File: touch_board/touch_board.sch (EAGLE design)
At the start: 43 parts, among them IC1 PIC18F47K42-I_PT, IC2 MAX203EEWP, K1 G6K-2P, X1 RS-232-1, X2 RS-232-2, X3 POWER, X4 GLORY, X5 Relay conn

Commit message: update
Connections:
- removed net N$59: C7.1, D2.A, R4.1
- new net N$62: C7.1, D2.A, R4.1, S3.1, S3.2, SV3.1
- net N$2: no longer S3.1, S3.2, SV3.1
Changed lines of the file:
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@@
 <wire x1="83.82" y1="-40.64" x2="83.82" y2="-43.18" width="0.1524" layer="91"/>
 <pinref part="SV2" gate="G$1" pin="4"/>
-<wire x1="83.82" y1="-20.32" x2="132.08" y2="-20.32" width="0.1524" layer="91"/>
+<wire x1="83.82" y1="-20.32" x2="137.16" y2="-20.32" width="0.1524" layer="91"/>
 <junction x="83.82" y="-20.32"/>
 <junction x="137.16" y="-20.32"/>
-<wire x1="132.08" y1="-20.32" x2="137.16" y2="-20.32" width="0.1524" layer="91"/>
-<wire x1="132.08" y1="-20.32" x2="132.08" y2="-30.48" width="0.1524" layer="91"/>
-<pinref part="SV3" gate="G$1" pin="1"/>
-<wire x1="132.08" y1="-30.48" x2="132.08" y2="-35.56" width="0.1524" layer="91"/>
-<wire x1="132.08" y1="-35.56" x2="137.16" y2="-35.56" width="0.1524" layer="91"/>
-<junction x="137.16" y="-35.56"/>
-<junction x="132.08" y="-20.32"/>
-<pinref part="S3" gate="G$1" pin="2"/>
-<pinref part="S3" gate="G$1" pin="1"/>
-<wire x1="165.1" y1="-55.88" x2="165.1" y2="-53.34" width="0.1524" layer="91"/>
-<wire x1="165.1" y1="-53.34" x2="165.1" y2="-50.8" width="0.1524" layer="91"/>
-<wire x1="165.1" y1="-50.8" x2="152.4" y2="-50.8" width="0.1524" layer="91"/>
-<wire x1="152.4" y1="-50.8" x2="152.4" y2="-30.48" width="0.1524" layer="91"/>
-<wire x1="152.4" y1="-30.48" x2="132.08" y2="-30.48" width="0.1524" layer="91"/>
-<junction x="132.08" y="-30.48"/>
-<junction x="165.1" y="-53.34"/>
-<junction x="165.1" y="-55.88"/>
 <pinref part="D2" gate="G$1" pin="C"/>
 <wire x1="71.12" y1="-20.32" x2="76.2" y2="-20.32" width="0.1524" layer="91"/>
@@
 </segment>
 </net>
-<net name="N$59" class="0">
-<segment>
+<net name="N$62" class="0">
+<segment>
+<pinref part="SV3" gate="G$1" pin="1"/>
+<junction x="137.16" y="-35.56"/>
+<wire x1="132.08" y1="-35.56" x2="137.16" y2="-35.56" width="0.1524" layer="91"/>
+<wire x1="132.08" y1="-35.56" x2="132.08" y2="-27.94" width="0.1524" layer="91"/>
+<wire x1="132.08" y1="-27.94" x2="152.4" y2="-27.94" width="0.1524" layer="91"/>
+<pinref part="S3" gate="G$1" pin="1"/>
+<pinref part="S3" gate="G$1" pin="2"/>
+<junction x="165.1" y="-55.88"/>
+<wire x1="165.1" y1="-55.88" x2="165.1" y2="-53.34" width="0.1524" layer="91"/>
+<junction x="165.1" y="-53.34"/>
+<wire x1="165.1" y1="-53.34" x2="165.1" y2="-50.8" width="0.1524" layer="91"/>
+<wire x1="165.1" y1="-50.8" x2="152.4" y2="-50.8" width="0.1524" layer="91"/>
+<wire x1="152.4" y1="-27.94" x2="152.4" y2="-50.8" width="0.1524" layer="91"/>
+<wire x1="152.4" y1="-50.8" x2="152.4" y2="-68.58" width="0.1524" layer="91"/>
+<wire x1="152.4" y1="-68.58" x2="53.34" y2="-68.58" width="0.1524" layer="91"/>
 <pinref part="C7" gate="G$1" pin="1"/>
 <pinref part="R4" gate="G$1" pin="1"/>
@@
 <pinref part="D2" gate="G$1" pin="A"/>
 <junction x="66.04" y="-20.32"/>
-</segment>
-</net>
+<wire x1="53.34" y1="-68.58" x2="53.34" y2="-20.32" width="0.1524" layer="91"/>
+<junction x="152.4" y="-50.8"/>
+</segment>
+</net>

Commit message: update
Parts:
- added C10: 0.1, rcl:C-USC0805
- added LED1: PWR ON, led:LEDCHIPLED_1206
- added PAD1: LCD9, wirepad:SMD2
- added PAD2: LCD10, wirepad:SMD2
- added R8: 220, rcl:R-US_R0805
- added SV8: LCD, con-lstb:MA10-1
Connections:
- new net N$63: IC1.RC4, SV5.5, SV8.1
- new net N$66: PAD1.P, SV8.9
- new net N$67: PAD2.P, SV8.10
- net N$33: now also SV8.6
- net N$34: now also SV8.4
- net N$35: now also SV8.5
- net N$36: now also SV8.3
- net N$37: now also LED1.A, R8.2; no longer IC1.RC4, SV5.5
- net N$38: now also SV8.2
- net VDD: now also C10.1, R8.1, SV8.7
- net VSS: now also C10.2, LED1.C, SV8.8

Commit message: update
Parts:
- added SV9: USBH, con-lstb:MA03-1
- added X6: MINI-USB-UX60A-MB-5ST, con-hirose:MINI-USB-UX60A-MB-5ST
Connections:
- new net N$59: SV9.3, X6.2
- new net N$61: SV9.2, X6.3
- new net N$64: SV9.1, X6.4
- net N$60: now also X6.1
- net VSS: now also X6.5
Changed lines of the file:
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@@
 <part name="LED1" library="led" library_urn="urn:adsk.eagle:library:259" deviceset="LED" device="CHIPLED_1206" package3d_urn="urn:adsk.eagle:package:15823/2" value="PWR ON"/>
 <part name="VSS26" library="supply1" library_urn="urn:adsk.eagle:library:371" deviceset="VSS" device=""/>
+<part name="VSS27" library="supply1" library_urn="urn:adsk.eagle:library:371" deviceset="VSS" device=""/>
+<part name="SV9" library="con-lstb" library_urn="urn:adsk.eagle:library:162" deviceset="MA03-1" device="" package3d_urn="urn:adsk.eagle:package:8339/1" value="USBH"/>
+<part name="X6" library="con-hirose" library_urn="urn:adsk.eagle:library:152" deviceset="MINI-USB-" device="UX60A-MB-5ST" package3d_urn="urn:adsk.eagle:package:7263/1"/>
 </parts>
 <sheets>
@@
 <instance part="VSS26" gate="G$1" x="104.14" y="-66.04" smashed="yes" rot="R90">
 <attribute name="VALUE" x="109.22" y="-68.58" size="1.778" layer="96" rot="R180"/>
+</instance>
+<instance part="VSS27" gate="G$1" x="182.88" y="-27.94" smashed="yes">
+<attribute name="VALUE" x="180.34" y="-33.02" size="1.778" layer="96" rot="R90"/>
+</instance>
+<instance part="SV9" gate="G$1" x="170.18" y="-20.32" smashed="yes">
+<attribute name="VALUE" x="168.91" y="-27.94" size="1.778" layer="96"/>
+<attribute name="NAME" x="168.91" y="-14.478" size="1.778" layer="95"/>
+</instance>
+<instance part="X6" gate="G$1" x="187.96" y="-20.32" smashed="yes">
+<attribute name="NAME" x="185.42" y="-8.89" size="1.778" layer="95"/>
+<attribute name="VALUE" x="198.12" y="-27.94" size="1.778" layer="96" rot="R90"/>
 </instance>
 </instances>
@@
 <pinref part="VSS26" gate="G$1" pin="VSS"/>
 <junction x="101.6" y="-66.04"/>
+</segment>
+<segment>
+<pinref part="VSS27" gate="G$1" pin="VSS"/>
+<pinref part="X6" gate="G$1" pin="5"/>
+<junction x="182.88" y="-25.4"/>
 </segment>
 </net>
@@
 <pinref part="D1" gate="G$1" pin="C"/>
 <junction x="127" y="-55.88"/>
+<wire x1="182.88" y1="-15.24" x2="160.02" y2="-7.62" width="0.1524" layer="91"/>
+<wire x1="160.02" y1="-7.62" x2="160.02" y2="-45.72" width="0.1524" layer="91"/>
+<wire x1="160.02" y1="-45.72" x2="127" y2="-45.72" width="0.1524" layer="91"/>
+<wire x1="127" y1="-45.72" x2="127" y2="-35.56" width="0.1524" layer="91"/>
+<wire x1="127" y1="-35.56" x2="109.22" y2="-35.56" width="0.1524" layer="91"/>
+<wire x1="109.22" y1="-35.56" x2="109.22" y2="-43.18" width="0.1524" layer="91"/>
+<pinref part="X6" gate="G$1" pin="1"/>
+<junction x="182.88" y="-15.24"/>
 </segment>
 </net>
@@
 </segment>
 </net>
+<net name="N$59" class="0">
+<segment>
+<pinref part="SV9" gate="G$1" pin="3"/>
+<wire x1="182.88" y1="-17.78" x2="177.8" y2="-17.78" width="0.1524" layer="91"/>
+<junction x="177.8" y="-17.78"/>
+<pinref part="X6" gate="G$1" pin="2"/>
+<junction x="182.88" y="-17.78"/>
+</segment>
+</net>
+<net name="N$61" class="0">
+<segment>
+<pinref part="SV9" gate="G$1" pin="2"/>
+<wire x1="182.88" y1="-20.32" x2="177.8" y2="-20.32" width="0.1524" layer="91"/>
+<junction x="177.8" y="-20.32"/>
+<pinref part="X6" gate="G$1" pin="3"/>
+<junction x="182.88" y="-20.32"/>
+</segment>
+</net>
+<net name="N$64" class="0">
+<segment>
+<pinref part="SV9" gate="G$1" pin="1"/>
+<wire x1="182.88" y1="-22.86" x2="177.8" y2="-22.86" width="0.1524" layer="91"/>
+<junction x="177.8" y="-22.86"/>
+<pinref part="X6" gate="G$1" pin="4"/>
+<junction x="182.88" y="-22.86"/>
+</segment>
+</net>

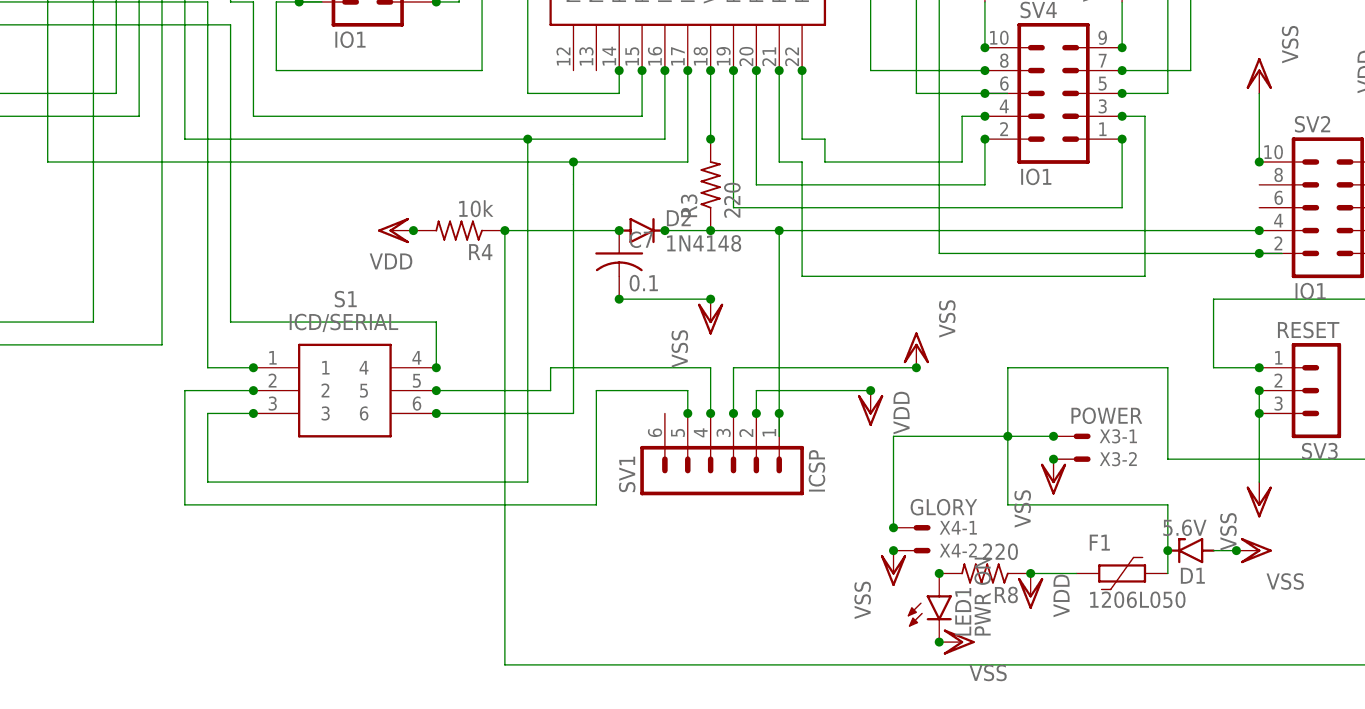
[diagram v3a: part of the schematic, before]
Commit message: update and fix switch pins on pcb
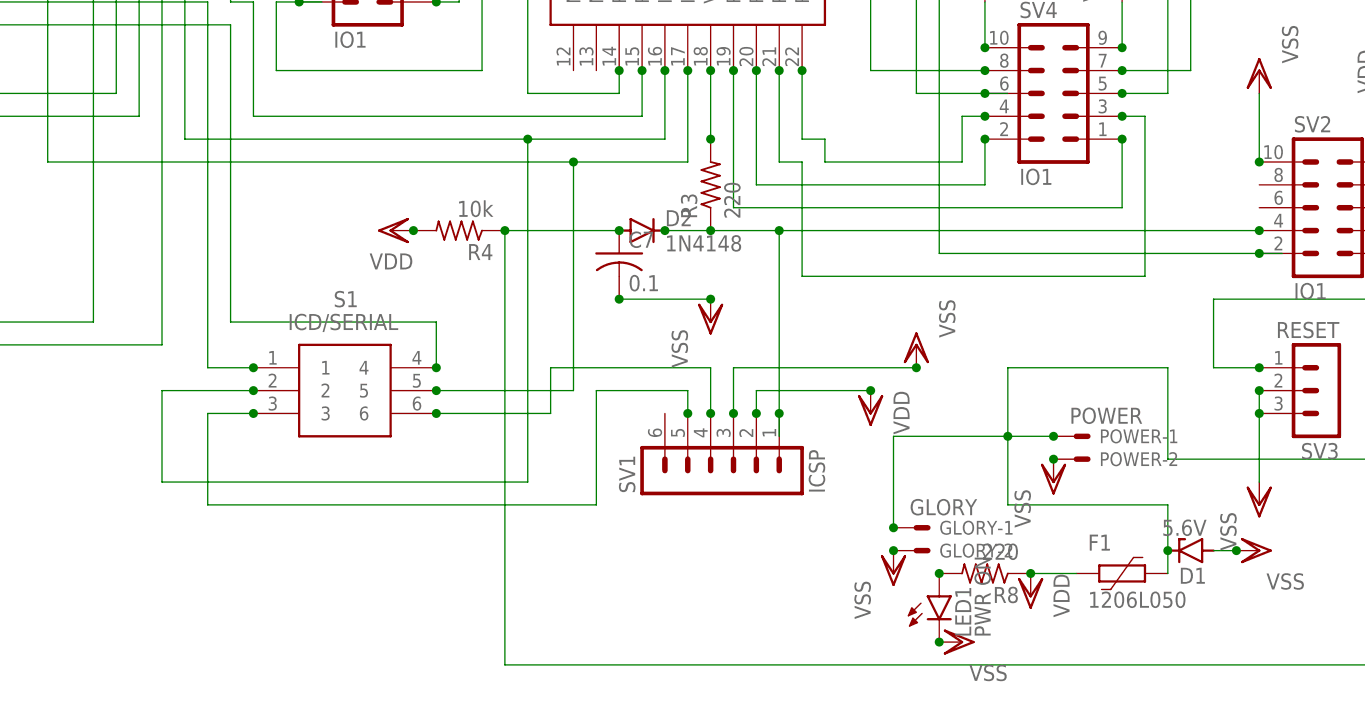
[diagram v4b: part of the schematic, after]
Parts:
- renumbered X3 to POWER, X4 to GLORY
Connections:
- removed net N$24: S1.2, SV1.5
- new net N$65: S1.3, SV1.5
- net N$23: now also S1.6; no longer S1.5
- net N$6: now also S1.5; no longer S1.6
- net N$7: now also S1.2; no longer S1.3
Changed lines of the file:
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@@
 <part name="P+2" library="supply1" library_urn="urn:adsk.eagle:library:371" deviceset="VCC" device=""/>
 <part name="P+3" library="supply1" library_urn="urn:adsk.eagle:library:371" deviceset="VCC" device=""/>
-<part name="X3" library="con-molex" library_urn="urn:adsk.eagle:library:165" deviceset="22-23-2021" device="" package3d_urn="urn:adsk.eagle:package:8078633/1" value="POWER"/>
+<part name="POWER" library="con-molex" library_urn="urn:adsk.eagle:library:165" deviceset="22-23-2021" device="" package3d_urn="urn:adsk.eagle:package:8078633/1" value="POWER"/>
 <part name="VSS13" library="supply1" library_urn="urn:adsk.eagle:library:371" deviceset="VSS" device=""/>
 <part name="C8" library="rcl" library_urn="urn:adsk.eagle:library:334" deviceset="C-US" device="C0805" package3d_urn="urn:adsk.eagle:package:23617/2" value="0.1"/>
@@
 <part name="VSS19" library="supply1" library_urn="urn:adsk.eagle:library:371" deviceset="VSS" device=""/>
 <part name="VDD12" library="supply1" library_urn="urn:adsk.eagle:library:371" deviceset="VDD" device=""/>
-<part name="X4" library="con-molex" library_urn="urn:adsk.eagle:library:165" deviceset="22-23-2021" device="" package3d_urn="urn:adsk.eagle:package:8078633/1" value="GLORY"/>
+<part name="GLORY" library="con-molex" library_urn="urn:adsk.eagle:library:165" deviceset="22-23-2021" device="" package3d_urn="urn:adsk.eagle:package:8078633/1" value="GLORY"/>
 <part name="VSS20" library="supply1" library_urn="urn:adsk.eagle:library:371" deviceset="VSS" device=""/>
 <part name="K1" library="relay" library_urn="urn:adsk.eagle:library:339" deviceset="G6K" device="-2P" package3d_urn="urn:adsk.eagle:package:24346/1"/>
@@
 <attribute name="VALUE" x="-10.16" y="-27.94" size="1.778" layer="96" rot="R90"/>
 </instance>
-<instance part="X3" gate="-1" x="116.84" y="-43.18" smashed="yes">
+<instance part="POWER" gate="-1" x="116.84" y="-43.18" smashed="yes">
 <attribute name="NAME" x="119.38" y="-43.942" size="1.524" layer="95"/>
 <attribute name="VALUE" x="116.078" y="-41.783" size="1.778" layer="96"/>
 </instance>
-<instance part="X3" gate="-2" x="116.84" y="-45.72" smashed="yes">
+<instance part="POWER" gate="-2" x="116.84" y="-45.72" smashed="yes">
 <attribute name="NAME" x="119.38" y="-46.482" size="1.524" layer="95"/>
 </instance>
@@
 <attribute name="VALUE" x="43.18" y="15.24" size="1.778" layer="96" rot="R90"/>
 </instance>
-<instance part="X4" gate="-1" x="99.06" y="-53.34" smashed="yes">
+<instance part="GLORY" gate="-1" x="99.06" y="-53.34" smashed="yes">
 <attribute name="NAME" x="101.6" y="-54.102" size="1.524" layer="95"/>
 <attribute name="VALUE" x="98.298" y="-51.943" size="1.778" layer="96"/>
 </instance>
-<instance part="X4" gate="-2" x="99.06" y="-55.88" smashed="yes">
+<instance part="GLORY" gate="-2" x="99.06" y="-55.88" smashed="yes">
 <attribute name="NAME" x="101.6" y="-56.642" size="1.524" layer="95"/>
 </instance>
@@
 </segment>
 <segment>
-<pinref part="X3" gate="-2" pin="S"/>
+<pinref part="POWER" gate="-2" pin="S"/>
 <pinref part="VSS13" gate="G$1" pin="VSS"/>
 <junction x="114.3" y="-45.72"/>
@@
 </segment>
 <segment>
-<pinref part="X4" gate="-2" pin="S"/>
+<pinref part="GLORY" gate="-2" pin="S"/>
 <pinref part="VSS20" gate="G$1" pin="VSS"/>
 <junction x="96.52" y="-55.88"/>
@@
 <wire x1="73.66" y1="-12.7" x2="60.96" y2="-12.7" width="0.1524" layer="91"/>
 <junction x="73.66" y="-2.54"/>
-<pinref part="S1" gate="G$1" pin="6"/>
-<wire x1="60.96" y1="-15.24" x2="60.96" y2="-40.64" width="0.1524" layer="91"/>
-<wire x1="60.96" y1="-40.64" x2="45.72" y2="-40.64" width="0.1524" layer="91"/>
-<junction x="45.72" y="-40.64"/>
+<wire x1="60.96" y1="-12.7" x2="60.96" y2="-38.1" width="0.1524" layer="91"/>
 <pinref part="SV7" gate="G$1" pin="8"/>
 <wire x1="30.48" y1="12.7" x2="2.54" y2="12.7" width="0.1524" layer="91"/>
 <wire x1="2.54" y1="12.7" x2="2.54" y2="-12.7" width="0.1524" layer="91"/>
 <wire x1="2.54" y1="-12.7" x2="60.96" y2="-12.7" width="0.1524" layer="91"/>
-<wire x1="60.96" y1="-12.7" x2="60.96" y2="-15.24" width="0.1524" layer="91"/>
 <junction x="60.96" y="-12.7"/>
 <junction x="30.48" y="12.7"/>
+<pinref part="S1" gate="G$1" pin="5"/>
+<wire x1="60.96" y1="-38.1" x2="45.72" y2="-38.1" width="0.1524" layer="91"/>
+<junction x="45.72" y="-38.1"/>
 </segment>
 </net>
@@
 <junction x="71.12" y="-2.54"/>
 <wire x1="55.88" y1="-10.16" x2="55.88" y2="-48.26" width="0.1524" layer="91"/>
-<wire x1="55.88" y1="-48.26" x2="20.32" y2="-48.26" width="0.1524" layer="91"/>
-<wire x1="20.32" y1="-48.26" x2="20.32" y2="-40.64" width="0.1524" layer="91"/>
-<wire x1="20.32" y1="-40.64" x2="25.4" y2="-40.64" width="0.1524" layer="91"/>
-<pinref part="S1" gate="G$1" pin="3"/>
-<junction x="25.4" y="-40.64"/>
+<wire x1="55.88" y1="-48.26" x2="15.24" y2="-48.26" width="0.1524" layer="91"/>
 <pinref part="SV7" gate="G$1" pin="7"/>
 <wire x1="45.72" y1="12.7" x2="55.88" y2="12.7" width="0.1524" layer="91"/>
@@
 <junction x="45.72" y="12.7"/>
 <junction x="55.88" y="-10.16"/>
+<pinref part="S1" gate="G$1" pin="2"/>
+<wire x1="15.24" y1="-38.1" x2="25.4" y2="-38.1" width="0.1524" layer="91"/>
+<junction x="25.4" y="-38.1"/>
+<wire x1="15.24" y1="-48.26" x2="15.24" y2="-38.1" width="0.1524" layer="91"/>
 </segment>
 </net>
@@
 </segment>
 </net>
-<net name="N$24" class="0">
-<segment>
-<pinref part="S1" gate="G$1" pin="2"/>
-<wire x1="17.78" y1="-38.1" x2="25.4" y2="-38.1" width="0.1524" layer="91"/>
-<wire x1="17.78" y1="-50.8" x2="17.78" y2="-38.1" width="0.1524" layer="91"/>
-<pinref part="SV1" gate="1" pin="5"/>
-<junction x="73.66" y="-40.64"/>
-<wire x1="73.66" y1="-38.1" x2="73.66" y2="-40.64" width="0.1524" layer="91"/>
-<wire x1="63.5" y1="-38.1" x2="73.66" y2="-38.1" width="0.1524" layer="91"/>
-<wire x1="63.5" y1="-38.1" x2="63.5" y2="-50.8" width="0.1524" layer="91"/>
-<wire x1="63.5" y1="-50.8" x2="17.78" y2="-50.8" width="0.1524" layer="91"/>
-<junction x="25.4" y="-38.1"/>
-</segment>
-</net>
 <net name="N$23" class="0">
 <segment>
-<pinref part="S1" gate="G$1" pin="5"/>
 <pinref part="SV1" gate="1" pin="4"/>
 <junction x="76.2" y="-40.64"/>
 <wire x1="76.2" y1="-35.56" x2="76.2" y2="-40.64" width="0.1524" layer="91"/>
 <wire x1="58.42" y1="-35.56" x2="76.2" y2="-35.56" width="0.1524" layer="91"/>
-<wire x1="58.42" y1="-35.56" x2="58.42" y2="-38.1" width="0.1524" layer="91"/>
-<wire x1="58.42" y1="-38.1" x2="45.72" y2="-38.1" width="0.1524" layer="91"/>
-<junction x="45.72" y="-38.1"/>
+<wire x1="58.42" y1="-35.56" x2="58.42" y2="-40.64" width="0.1524" layer="91"/>
+<pinref part="S1" gate="G$1" pin="6"/>
+<wire x1="58.42" y1="-40.64" x2="45.72" y2="-40.64" width="0.1524" layer="91"/>
+<junction x="45.72" y="-40.64"/>
 </segment>
 </net>
@@
 <wire x1="127" y1="-55.88" x2="127" y2="-50.8" width="0.1524" layer="91"/>
 <wire x1="127" y1="-50.8" x2="109.22" y2="-50.8" width="0.1524" layer="91"/>
-<pinref part="X4" gate="-1" pin="S"/>
+<pinref part="GLORY" gate="-1" pin="S"/>
 <wire x1="96.52" y1="-53.34" x2="96.52" y2="-43.18" width="0.1524" layer="91"/>
-<pinref part="X3" gate="-1" pin="S"/>
+<pinref part="POWER" gate="-1" pin="S"/>
 <wire x1="96.52" y1="-43.18" x2="109.22" y2="-43.18" width="0.1524" layer="91"/>
 <wire x1="109.22" y1="-43.18" x2="114.3" y2="-43.18" width="0.1524" layer="91"/>
@@
 </segment>
 </net>
+<net name="N$65" class="0">
+<segment>
+<wire x1="20.32" y1="-40.64" x2="25.4" y2="-40.64" width="0.1524" layer="91"/>
+<pinref part="S1" gate="G$1" pin="3"/>
+<junction x="25.4" y="-40.64"/>
+<pinref part="SV1" gate="1" pin="5"/>
+<junction x="73.66" y="-40.64"/>
+<wire x1="73.66" y1="-38.1" x2="73.66" y2="-40.64" width="0.1524" layer="91"/>
+<wire x1="63.5" y1="-38.1" x2="73.66" y2="-38.1" width="0.1524" layer="91"/>
+<wire x1="63.5" y1="-38.1" x2="63.5" y2="-50.8" width="0.1524" layer="91"/>
+<wire x1="63.5" y1="-50.8" x2="20.32" y2="-50.8" width="0.1524" layer="91"/>
+<wire x1="20.32" y1="-40.64" x2="20.32" y2="-50.8" width="0.1524" layer="91"/>
+</segment>
+</net>

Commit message: update
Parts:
- removed S1: ICD/SERIAL, JS202011SCQN:JS202011SCQN
- added ICSP/SERIAL: JS202011SCQN, JS202011SCQN_fixed:JS202011SCQN
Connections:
- net N$20: now also ICSP/SERIAL.1, XT1.C; no longer R6.2, S1.1
- net N$22: now also ICSP/SERIAL.4; no longer S1.4
- net N$23: now also ICSP/SERIAL.6; no longer S1.6
- net N$6: now also ICSP/SERIAL.5; no longer S1.5
- net N$65: now also ICSP/SERIAL.3; no longer S1.3
- net N$7: now also ICSP/SERIAL.2; no longer S1.2
- net VDD: now also R6.2
- net VSS: no longer XT1.C
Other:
- moved on the sheet: R6
